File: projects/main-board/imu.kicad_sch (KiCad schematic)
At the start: 3 parts

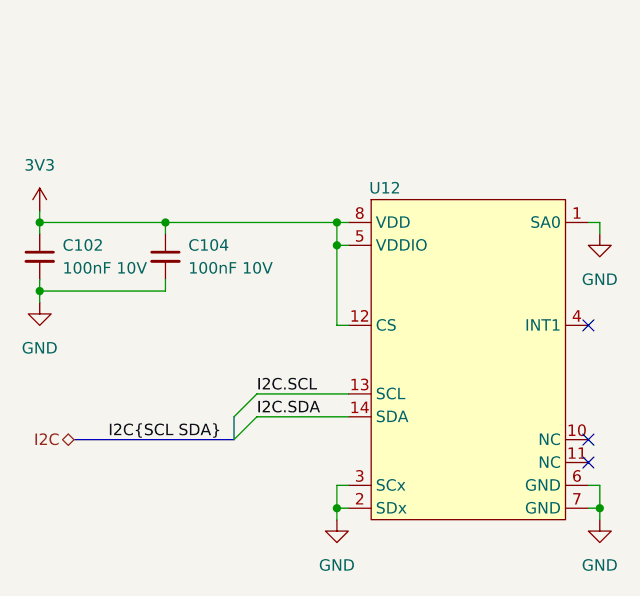
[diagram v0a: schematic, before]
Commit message: Updated schematics with new symbols
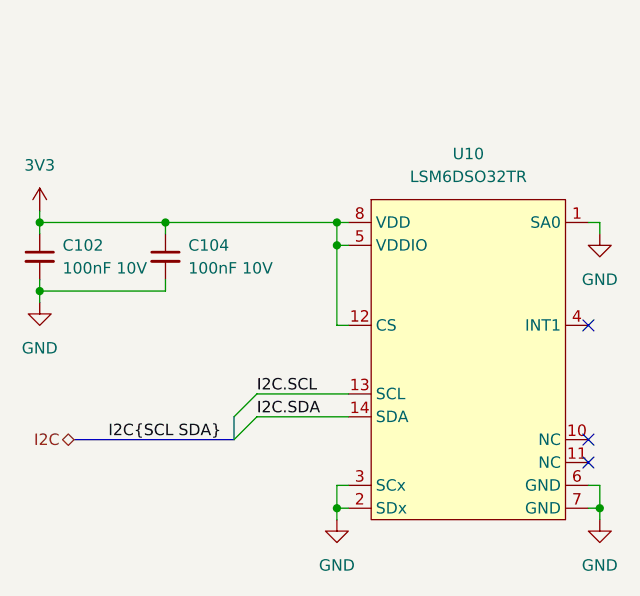
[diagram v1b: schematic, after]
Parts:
- removed U12: ~, symbol symbol-library:LSM6DSO32TR
- added U10: LSM6DSO32TR, footprint-library:LSM6DSO32TR, symbol symbol-library:LSM6DSO32TR
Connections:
- net 3V3: now also U10.12 (CS), U10.5 (VDDIO), U10.8 (VDD)
- net GND: now also U10.1 (SA0), U10.2 (SDx), U10.3 (SCx), U10.6 (GND), U10.7 (GND)
- net I2C.SCL: now also U10.13 (SCL)
- net I2C.SDA: now also U10.14 (SDA)
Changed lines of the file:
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@@
+	)
+	(symbol
+		(lib_name "LSM6DSO32TR_1")
+		(lib_id "symbol-library:LSM6DSO32TR")
+		(at 148.59 83.82 0)
+		(unit 1)
+		(exclude_from_sim no)
+		(in_bom yes)
+		(on_board yes)
+		(dnp no)
+		(fields_autoplaced yes)
+		(property "Reference" "U10"
+			(at 159.385 78.74 0)
+			(effects
+				(font
+					(size 1.27 1.27)
+				)
+			)
+		)
+		(property "Value" "LSM6DSO32TR"
+			(at 159.385 81.28 0)
+			(effects
+				(font
+					(size 1.27 1.27)
+				)
+			)
+		)
+		(property "Footprint" "footprint-library:LSM6DSO32TR"
+			(at 161.29 122.428 0)
+			(effects
+				(font
+					(size 1.27 1.27)
+				)
+				(hide yes)
+			)
+		)
+		(property "Datasheet" ""
+			(at 148.59 83.82 0)
+			(effects
+				(font
+					(size 1.27 1.27)
+				)
+				(hide yes)
+			)
+		)
+		(property "Description" ""
+			(at 148.59 83.82 0)
+			(effects
+				(font
+					(size 1.27 1.27)
+				)
+				(hide yes)
+			)
+		)
+		(pin "8"
+		)
+		(pin "5"
+		)
+		(pin "12"
+		)
+		(pin "13"
+		)
+		(pin "14"
+		)
+		(pin "3"
+		)
+		(pin "2"
+		)
+		(pin "1"
+		)
+		(pin "4"
+		)
+		(pin "10"
+		)
+		(pin "11"
+		)
+		(pin "6"
+		)
+		(pin "7"
+		)
+		(instances
+			(project ""
+				(path "/c621b5fd-2ef7-4a67-960d-0ffc72b1245a/04d71d97-5afb-4bae-a39c-935e2e9f31b5"
+					(reference "U10")
+					(unit 1)
+				)
+			)
+		)
 	)
 	(symbol
@@
 					(unit 1)
 				)
-			)
-		)
-	)
-	(symbol
-		(lib_id "symbol-library:LSM6DSO32TR")
-		(at 148.59 83.82 0)
-		(unit 1)
-		(exclude_from_sim no)
-		(in_bom yes)
-		(on_board yes)
-		(dnp no)
-		(property "Reference" "U12"
-			(at 150.114 82.55 0)
-			(effects
-				(font
-					(size 1.27 1.27)
-				)
-			)
-		)
-		(property "Value" "~"
-			(at 154.178 82.296 0)
-			(effects
-				(font
-					(size 1.27 1.27)
-				)
-			)
-		)
-		(property "Footprint" ""
-			(at 148.59 83.82 0)
-			(effects
-				(font
-					(size 1.27 1.27)
-				)
-				(hide yes)
-			)
-		)
-		(property "Datasheet" ""
-			(at 148.59 83.82 0)
-			(effects
-				(font
-					(size 1.27 1.27)
-				)
-				(hide yes)
-			)
-		)
-		(property "Description" ""
-			(at 148.59 83.82 0)
-			(effects
-				(font
-					(size 1.27 1.27)
-				)
-				(hide yes)
-			)
-		)
-		(pin "11"
-		)
-		(pin "6"
-		)
-		(pin "7"
-		)
-		(pin "3"
-		)
-		(pin "2"
-		)
-		(pin "1"
-		)
-		(pin "4"
-		)
-		(pin "10"
-		)
-		(pin "14"
-		)
-		(pin "13"
-		)
-		(pin "5"
-		)
-		(pin "8"
-		)
-		(pin "12"
-		)
-		(instances
-			(project ""
-				(path "/c621b5fd-2ef7-4a67-960d-0ffc72b1245a/04d71d97-5afb-4bae-a39c-935e2e9f31b5"
-					(reference "U12")
-					(unit 1)
-				)

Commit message: Re-annotate schematics.
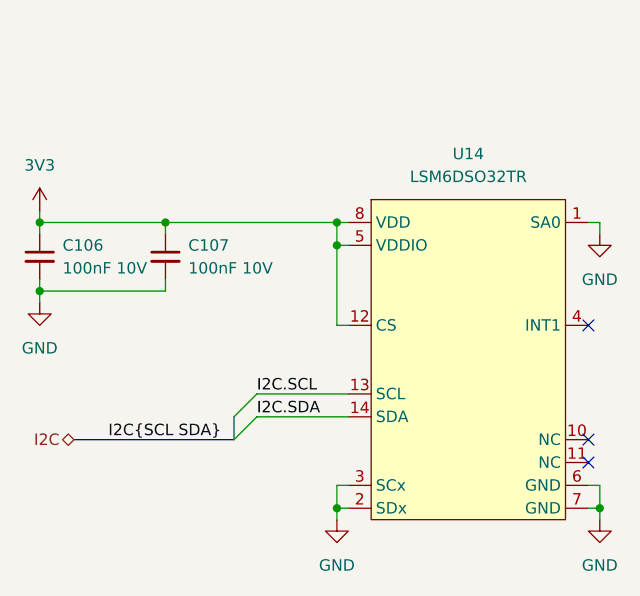
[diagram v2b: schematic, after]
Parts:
- renumbered C102 to C106, C104 to C107, U10 to U14
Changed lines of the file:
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@@
 		(dnp no)
 		(fields_autoplaced yes)
-		(property "Reference" "#PWR0132"
+		(property "Reference" "#PWR0153"
 			(at 111.76 88.9 0)
 			(effects
@@
 			(project ""
 				(path "/c621b5fd-2ef7-4a67-960d-0ffc72b1245a/04d71d97-5afb-4bae-a39c-935e2e9f31b5"
-					(reference "#PWR0132")
+					(reference "#PWR0153")
 					(unit 1)
 				)
@@
 		(dnp no)
 		(fields_autoplaced yes)
-		(property "Reference" "#PWR0135"
+		(property "Reference" "#PWR0156"
 			(at 173.99 93.98 0)
 			(effects
@@
 			(project "main-board"
 				(path "/c621b5fd-2ef7-4a67-960d-0ffc72b1245a/04d71d97-5afb-4bae-a39c-935e2e9f31b5"
-					(reference "#PWR0135")
+					(reference "#PWR0156")
 					(unit 1)
 				)
@@
 		(dnp no)
 		(fields_autoplaced yes)
-		(property "Reference" "#PWR0134"
+		(property "Reference" "#PWR0157"
 			(at 173.99 125.73 0)
 			(effects
@@
 			(project ""
 				(path "/c621b5fd-2ef7-4a67-960d-0ffc72b1245a/04d71d97-5afb-4bae-a39c-935e2e9f31b5"
-					(reference "#PWR0134")
+					(reference "#PWR0157")
 					(unit 1)
 				)
@@
 		(dnp no)
 		(fields_autoplaced yes)
-		(property "Reference" "C104"
+		(property "Reference" "C107"
 			(at 128.27 88.9062 0)
 			(effects
@@
 			(project "main-board"
 				(path "/c621b5fd-2ef7-4a67-960d-0ffc72b1245a/04d71d97-5afb-4bae-a39c-935e2e9f31b5"
-					(reference "C104")
+					(reference "C107")
 					(unit 1)
 				)
@@
 		(dnp no)
 		(fields_autoplaced yes)
-		(property "Reference" "#PWR0136"
+		(property "Reference" "#PWR0154"
 			(at 111.76 101.6 0)
 			(effects
@@
 			(project "main-board"
 				(path "/c621b5fd-2ef7-4a67-960d-0ffc72b1245a/04d71d97-5afb-4bae-a39c-935e2e9f31b5"
-					(reference "#PWR0136")
+					(reference "#PWR0154")
 					(unit 1)
 				)
@@
 		(dnp no)
 		(fields_autoplaced yes)
-		(property "Reference" "U10"
+		(property "Reference" "U14"
 			(at 159.385 78.74 0)
 			(effects
@@
 			(project ""
 				(path "/c621b5fd-2ef7-4a67-960d-0ffc72b1245a/04d71d97-5afb-4bae-a39c-935e2e9f31b5"
-					(reference "U10")
+					(reference "U14")
 					(unit 1)
 				)
@@
 		(dnp no)
 		(fields_autoplaced yes)
-		(property "Reference" "#PWR0137"
+		(property "Reference" "#PWR0155"
 			(at 144.78 125.73 0)
 			(effects
@@
 			(project "main-board"
 				(path "/c621b5fd-2ef7-4a67-960d-0ffc72b1245a/04d71d97-5afb-4bae-a39c-935e2e9f31b5"
-					(reference "#PWR0137")
+					(reference "#PWR0155")
 					(unit 1)
 				)
@@
 		(dnp no)
 		(fields_autoplaced yes)
-		(property "Reference" "C102"
+		(property "Reference" "C106"
 			(at 114.3 88.9062 0)
 			(effects
@@
 			(project ""
 				(path "/c621b5fd-2ef7-4a67-960d-0ffc72b1245a/04d71d97-5afb-4bae-a39c-935e2e9f31b5"
-					(reference "C102")
-					(unit 1)
-				)
+					(reference "C106")
+					(unit 1)
+				)

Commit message: Normalise capacitors
- Add capacitor parts to library.
- Replace all placeholder capacitors
  with the actual part numbers.
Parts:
- removed C106, C107: 100nF 10V, symbol Device:C_Small
- added C106, C107: 100nF 10V, Capacitor_SMD:C_0402_1005Metric, symbol symbol-library-capacitors:CC0402KRX7R6BB104
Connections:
- net 3V3: now also C106.1, C107.1
- net GND: now also C106.2, C107.2
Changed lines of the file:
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@@
 		(dnp no)
 		(fields_autoplaced yes)
-		(property "Reference" "#PWR0153"
+		(property "Reference" "#PWR0151"
 			(at 111.76 88.9 0)
 			(effects
@@
 			(project ""
 				(path "/c621b5fd-2ef7-4a67-960d-0ffc72b1245a/04d71d97-5afb-4bae-a39c-935e2e9f31b5"
-					(reference "#PWR0153")
+					(reference "#PWR0151")
 					(unit 1)
 				)
@@
 		(dnp no)
 		(fields_autoplaced yes)
-		(property "Reference" "#PWR0156"
+		(property "Reference" "#PWR0154"
 			(at 173.99 93.98 0)
 			(effects
@@
 			(project "main-board"
 				(path "/c621b5fd-2ef7-4a67-960d-0ffc72b1245a/04d71d97-5afb-4bae-a39c-935e2e9f31b5"
-					(reference "#PWR0156")
+					(reference "#PWR0154")
 					(unit 1)
 				)
@@
 		(dnp no)
 		(fields_autoplaced yes)
-		(property "Reference" "#PWR0157"
+		(property "Reference" "#PWR0155"
 			(at 173.99 125.73 0)
 			(effects
@@
 			(project ""
 				(path "/c621b5fd-2ef7-4a67-960d-0ffc72b1245a/04d71d97-5afb-4bae-a39c-935e2e9f31b5"
-					(reference "#PWR0157")
-					(unit 1)
-				)
-			)
-		)
-	)
-	(symbol
-		(lib_id "Device:C_Small")
-		(at 125.73 90.17 0)
-		(unit 1)
-		(exclude_from_sim no)
-		(in_bom yes)
-		(on_board yes)
-		(dnp no)
-		(fields_autoplaced yes)
-		(property "Reference" "C107"
-			(at 128.27 88.9062 0)
+					(reference "#PWR0155")
+					(unit 1)
+				)
+			)
+		)
+	)
+	(symbol
+		(lib_id "symbol-library-capacitors:CC0402KRX7R6BB104")
+		(at 111.76 90.17 0)
+		(unit 1)
+		(exclude_from_sim no)
+		(in_bom yes)
+		(on_board yes)
+		(dnp no)
+		(fields_autoplaced yes)
+		(property "Reference" "C106"
+			(at 114.3 88.9062 0)
 			(effects
 				(font
@@
 		)
 		(property "Value" "100nF 10V"
-			(at 128.27 91.4462 0)
+			(at 114.3 91.4462 0)
 			(effects
 				(font
@@
 			)
 		)
-		(property "Footprint" ""
-			(at 125.73 90.17 0)
+		(property "Footprint" "Capacitor_SMD:C_0402_1005Metric"
+			(at 111.76 90.17 0)
 			(effects
 				(font
@@
 		)
 		(property "Datasheet" "~"
-			(at 125.73 90.17 0)
+			(at 111.76 90.17 0)
 			(effects
 				(font
@@
 		)
 		(property "Description" "Unpolarized capacitor, small symbol"
-			(at 125.73 90.17 0)
+			(at 111.76 90.17 0)
 			(effects
 				(font
@@
 			(project "main-board"
 				(path "/c621b5fd-2ef7-4a67-960d-0ffc72b1245a/04d71d97-5afb-4bae-a39c-935e2e9f31b5"
-					(reference "C107")
+					(reference "C106")
 					(unit 1)
 				)
@@
 		(dnp no)
 		(fields_autoplaced yes)
-		(property "Reference" "#PWR0154"
+		(property "Reference" "#PWR0152"
 			(at 111.76 101.6 0)
 			(effects
@@
 			(project "main-board"
 				(path "/c621b5fd-2ef7-4a67-960d-0ffc72b1245a/04d71d97-5afb-4bae-a39c-935e2e9f31b5"
-					(reference "#PWR0154")
+					(reference "#PWR0152")
 					(unit 1)
 				)
@@
 		(dnp no)
 		(fields_autoplaced yes)
-		(property "Reference" "#PWR0155"
+		(property "Reference" "#PWR0153"
 			(at 144.78 125.73 0)
 			(effects
@@
 			(project "main-board"
 				(path "/c621b5fd-2ef7-4a67-960d-0ffc72b1245a/04d71d97-5afb-4bae-a39c-935e2e9f31b5"
-					(reference "#PWR0155")
-					(unit 1)
-				)
-			)
-		)
-	)
-	(symbol
-		(lib_id "Device:C_Small")
-		(at 111.76 90.17 0)
-		(unit 1)
-		(exclude_from_sim no)
-		(in_bom yes)
-		(on_board yes)
-		(dnp no)
-		(fields_autoplaced yes)
-		(property "Reference" "C106"
-			(at 114.3 88.9062 0)
+					(reference "#PWR0153")
+					(unit 1)
+				)
+			)
+		)
+	)
+	(symbol
+		(lib_id "symbol-library-capacitors:CC0402KRX7R6BB104")
+		(at 125.73 90.17 0)
+		(unit 1)
+		(exclude_from_sim no)
+		(in_bom yes)
+		(on_board yes)
+		(dnp no)
+		(fields_autoplaced yes)
+		(property "Reference" "C107"
+			(at 128.27 88.9062 0)
 			(effects
 				(font
@@
 		)
 		(property "Value" "100nF 10V"
-			(at 114.3 91.4462 0)
+			(at 128.27 91.4462 0)
 			(effects
 				(font
@@
 			)
 		)
-		(property "Footprint" ""
-			(at 111.76 90.17 0)
+		(property "Footprint" "Capacitor_SMD:C_0402_1005Metric"
+			(at 125.73 90.17 0)
 			(effects
 				(font
@@
 		)
 		(property "Datasheet" "~"
-			(at 111.76 90.17 0)
+			(at 125.73 90.17 0)
 			(effects
 				(font
@@
 		)
 		(property "Description" "Unpolarized capacitor, small symbol"
-			(at 111.76 90.17 0)
+			(at 125.73 90.17 0)
 			(effects
 				(font
@@
 		)
 		(instances
-			(project ""
-				(path "/c621b5fd-2ef7-4a67-960d-0ffc72b1245a/04d71d97-5afb-4bae-a39c-935e2e9f31b5"
-					(reference "C106")
-					(unit 1)
-				)
+			(project "main-board"
+				(path "/c621b5fd-2ef7-4a67-960d-0ffc72b1245a/04d71d97-5afb-4bae-a39c-935e2e9f31b5"
+					(reference "C107")
+					(unit 1)
+				)

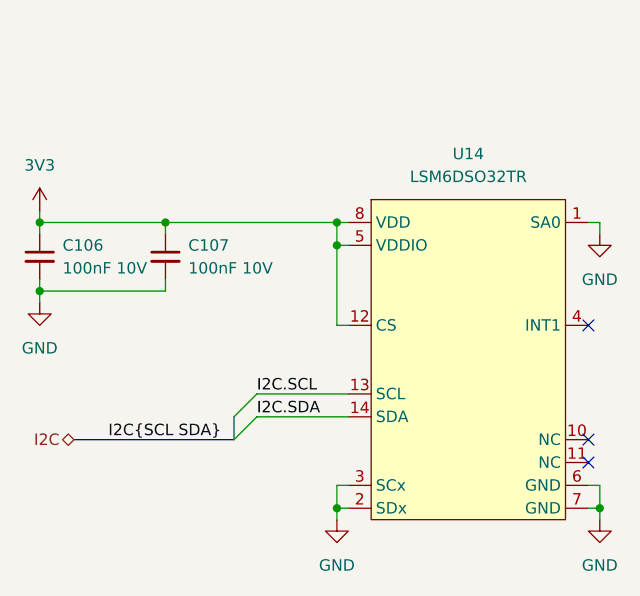
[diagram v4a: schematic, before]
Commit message: Fix footprint DRC errors.
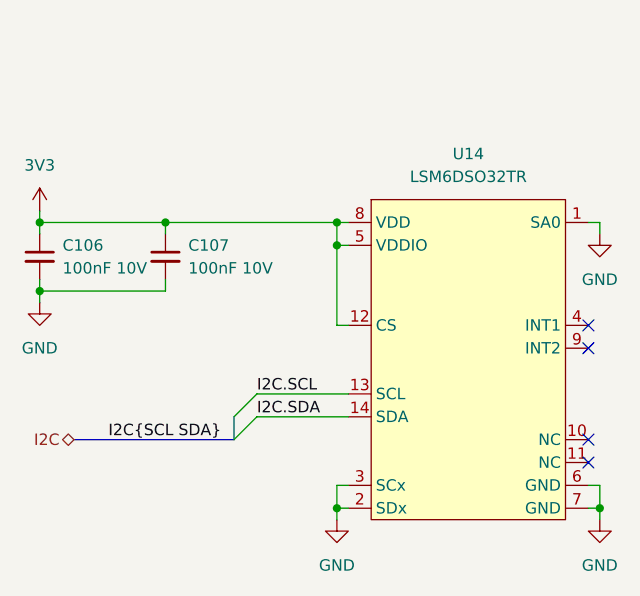
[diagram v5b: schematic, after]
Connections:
- no-connect marks 3 -> 4
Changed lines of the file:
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@@
+	)
+	(no_connect
+		(at 172.72 100.33)
 	)
 	(no_connect
@@
 	)
 	(symbol
-		(lib_name "LSM6DSO32TR_1")
 		(lib_id "symbol-library:LSM6DSO32TR")
 		(at 148.59 83.82 0)
@@
 		(pin "7"
 		)
+		(pin "9"
+		)
 		(instances

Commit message: WIP splitting main board into 3
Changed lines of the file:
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@@
 		(at 172.72 113.03)
 	)
-	(bus_entry
-		(at 135.89 105.41)
-		(size -2.54 2.54)
-		(stroke
-			(width 0)
-			(type default)
-		)
-	)
-	(bus_entry
-		(at 135.89 107.95)
-		(size -2.54 2.54)
-		(stroke
-			(width 0)
-			(type default)
-		)
-	)
 	(wire
 		(pts
@@
 	(bus
 		(pts
-			(xy 115.57 110.49) (xy 133.35 110.49)
+			(xy 115.57 66.04) (xy 133.35 66.04)
 		)
 		(stroke
@@
 		(pts
 			(xy 146.05 97.79) (xy 144.78 97.79)
-		)
-		(stroke
-			(width 0)
-			(type default)
-		)
-	)
-	(bus
-		(pts
-			(xy 133.35 107.95) (xy 133.35 110.49)
 		)
 		(stroke
@@
 	)
 	(label "I2C{SCL SDA}"
-		(at 119.38 110.49 0)
+		(at 119.38 66.04 0)
 		(effects
 			(font
@@
 	(hierarchical_label "I2C"
 		(shape bidirectional)
-		(at 115.57 110.49 180)
-		(effects
-			(font
+		(at 115.57 66.04 180)
+		(effects
+			(font
